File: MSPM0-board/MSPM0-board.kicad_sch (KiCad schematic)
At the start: 13 parts, among them J1 USB_C_Receptacle_USB2.0_16P, U1 MSPM0G3507SPTR, U2 USBLC6-2SC6, X1 8MHz

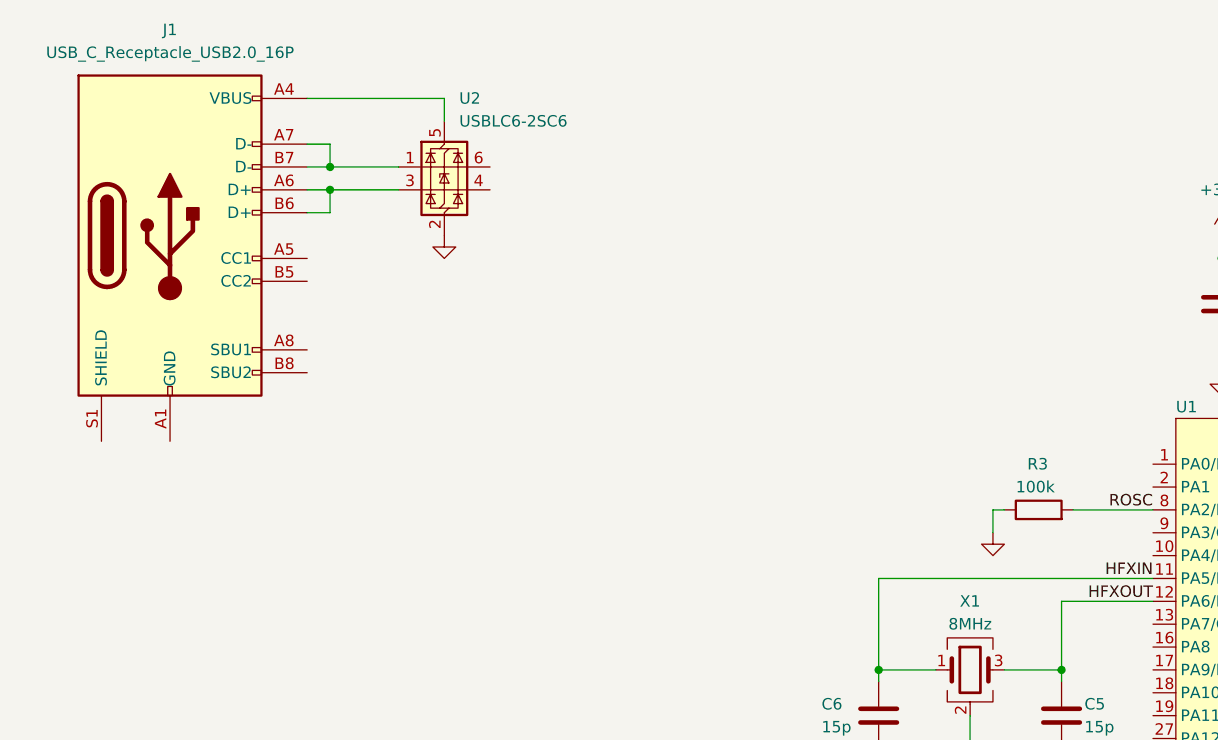
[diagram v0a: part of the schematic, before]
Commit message: mspm0(feat): add power supply circuit
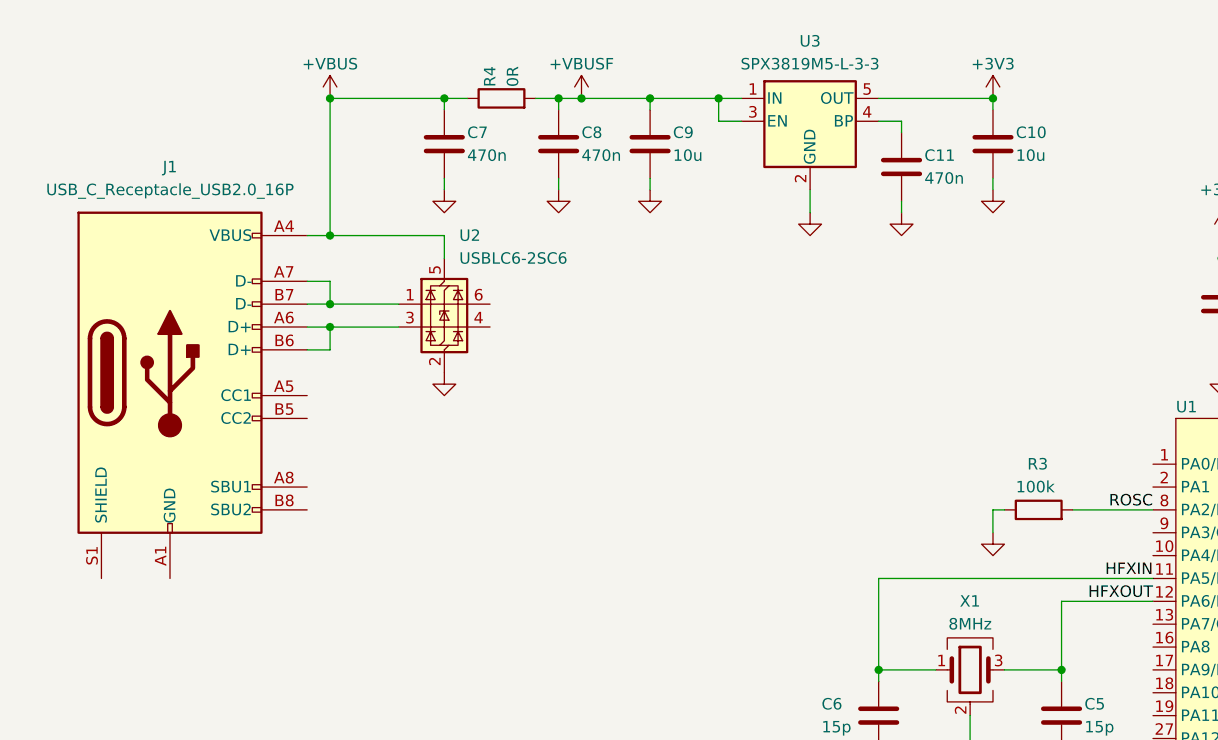
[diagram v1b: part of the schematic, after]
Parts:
- added C10, C9: 10u, Capacitor_SMD:C_0805_2012Metric, symbol Device:C
- added C11, C7, C8: 470n, Capacitor_SMD:C_0603_1608Metric, symbol Device:C
- added R4: 0R, Resistor_SMD:R_0603_1608Metric, symbol Device:R
- added U3: SPX3819M5-L-3-3, Package_TO_SOT_SMD:SOT-23-5, symbol Regulator_Linear:SPX3819M5-L-3-3
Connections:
- net +3V3: now also C10.1, U3.5 (OUT)
- net GND: now also C10.2, C11.2, C7.2, C8.2, C9.2, U3.2 (GND)
- net +VBUS: now reaches J1.A4 (VBUS), J1.A9 (VBUS), J1.B4 (VBUS), J1.B9 (VBUS), U2.5 (VBUS)
- net +VBUS: now also C7.1, R4.1
- new net: C11.1, U3.4 (BP)
- new net +VBUSF: C8.1, C9.1, R4.2, U3.1 (IN), U3.3 (EN)
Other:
- moved on the sheet: J1, U2

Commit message: mspm0(feat): finish usb
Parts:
- added R5, R6: 5k1, Resistor_SMD:R_0603_1608Metric, symbol Device:R
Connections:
- net GND: now also J1.A1 (GND), J1.A12 (GND), J1.B1 (GND), J1.B12 (GND), J1.S1 (SHIELD), R5.2, R6.2
- net at J1.A5 (CC1): now also R6.1
- net USBD+: now reaches J1.A6 (D+), J1.B6 (D+), U2.3 (I/O2)
- net USBD-: now reaches J1.A7 (D-), J1.B7 (D-), U2.1 (I/O1)
- net at J1.B5 (CC2): now also R5.1
- no-connect marks 0 -> 2
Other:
- moved on the sheet: U2

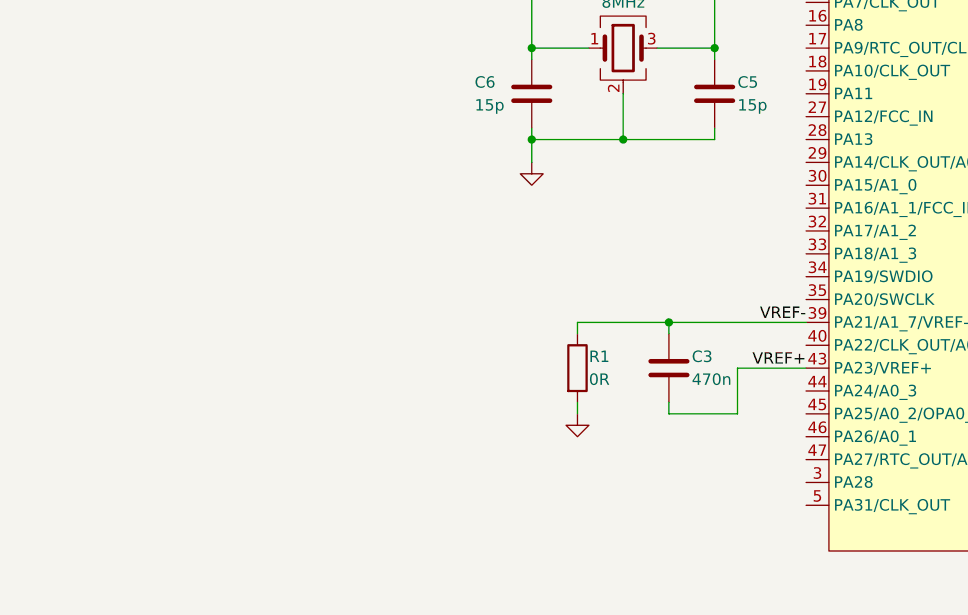
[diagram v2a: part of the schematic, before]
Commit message: mspm0(feat): add swd connector
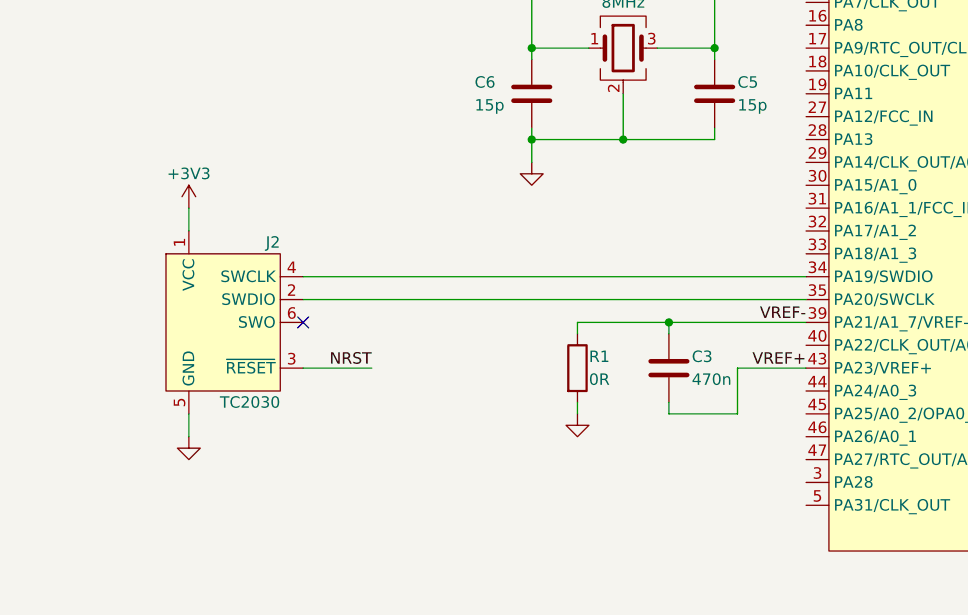
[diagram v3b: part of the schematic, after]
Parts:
- added J2: TC2030, Connector:Tag-Connect_TC2030-IDC-FP_2x03_P1.27mm_Vertical, symbol Connector:Conn_ARM_SWD_TagConnect_TC2030
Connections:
- net +3V3: now also J2.1 (VCC)
- net GND: now also J2.5 (GND)
- net NRST: now also J2.3 (~{RESET})
- net at U1.34 (PA19/SWDIO): now also J2.4 (SWCLK)
- net at U1.35 (PA20/SWCLK): now also J2.2 (SWDIO)
- no-connect marks 2 -> 3

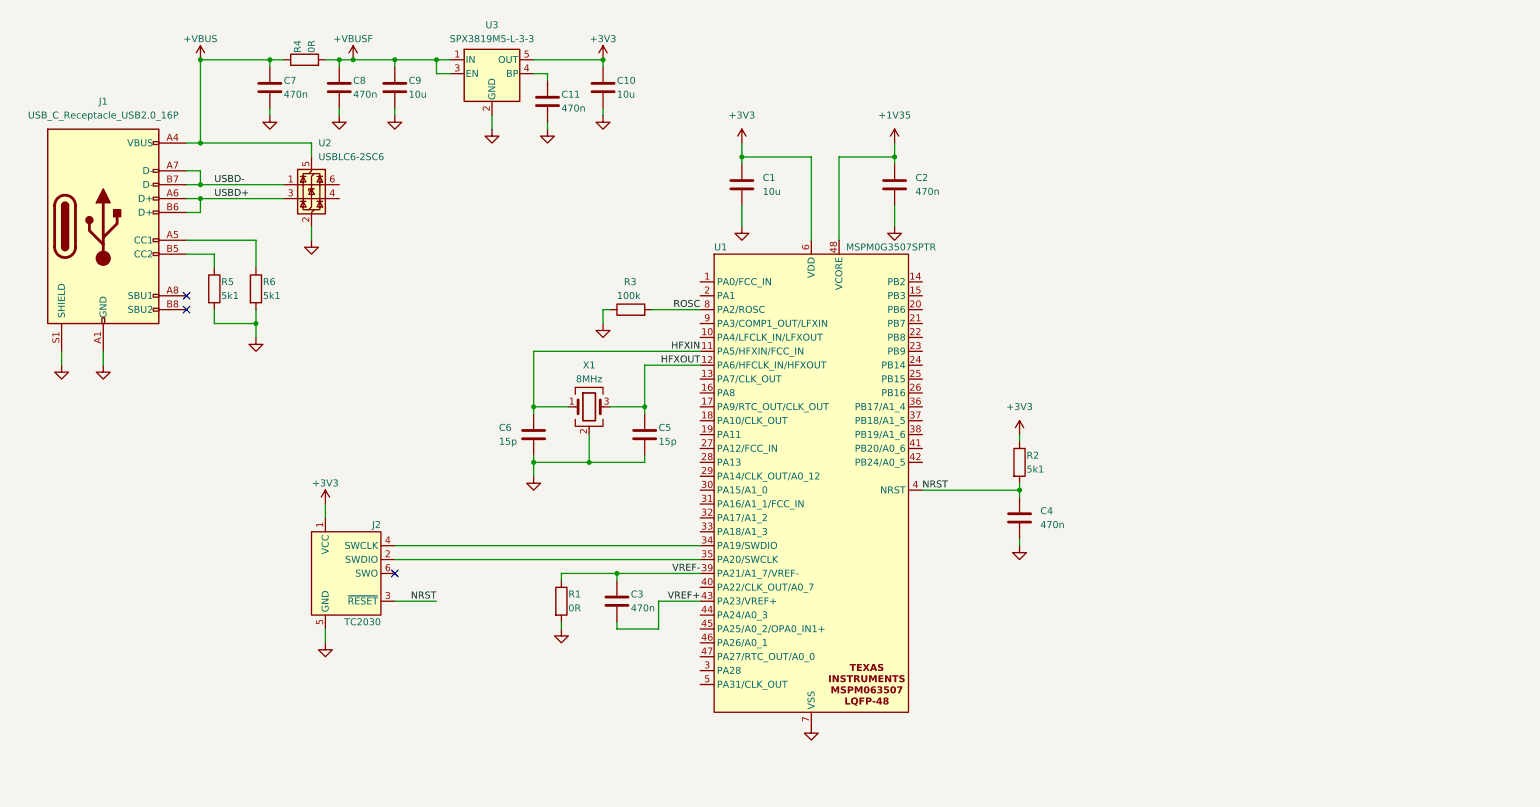
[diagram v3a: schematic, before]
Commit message: mspm0(feat): add usb to uart converter
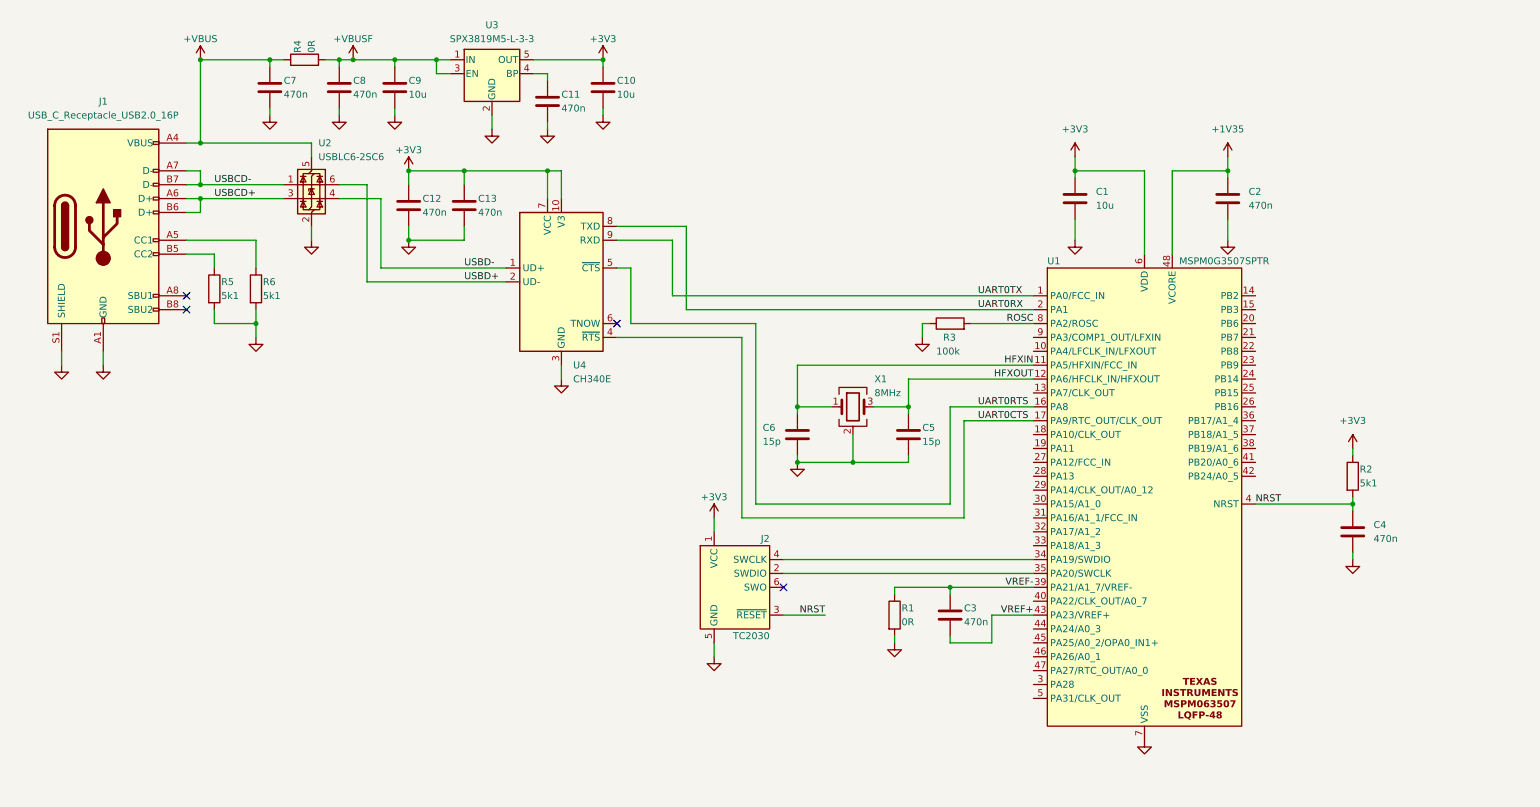
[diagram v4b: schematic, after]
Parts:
- added C12, C13: 470n, Capacitor_SMD:C_0603_1608Metric, symbol Device:C
- added U4: CH340E, Package_SO:MSOP-10_3x3mm_P0.5mm, symbol Interface_USB:CH340E
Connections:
- net +3V3: now also C12.1, C13.1, U4.10 (V3), U4.7 (VCC)
- net GND: now also C12.2, C13.2, U4.3 (GND)
- net USBD+: now also U2.6 (I/O1), U4.2 (UD-); no longer J1.A6 (D+), J1.B6 (D+), U2.3 (I/O2)
- net USBD-: now also U2.4 (I/O2), U4.1 (UD+); no longer J1.A7 (D-), J1.B7 (D-), U2.1 (I/O1)
- net UART0TX: now reaches U1.1 (PA0/FCC_IN)
- net UART0TX: now also U4.9 (RXD)
- net UART0RTS: now reaches U1.16 (PA8)
- net UART0RTS: now also U4.5 (~{CTS})
- net UART0CTS: now reaches U1.17 (PA9/RTC_OUT/CLK_OUT)
- net UART0CTS: now also U4.4 (~{RTS})
- net UART0RX: now reaches U1.2 (PA1)
- net UART0RX: now also U4.8 (TXD)
- new net USBCD+: J1.A6 (D+), J1.B6 (D+), U2.3 (I/O2)
- new net USBCD-: J1.A7 (D-), J1.B7 (D-), U2.1 (I/O1)
- no-connect marks 3 -> 4
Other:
- moved on the sheet: C1, C2, C3, C4, C5, C6, J2, R1, R2, R3, U1, X1

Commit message: mspm0(feat): add accelerometer
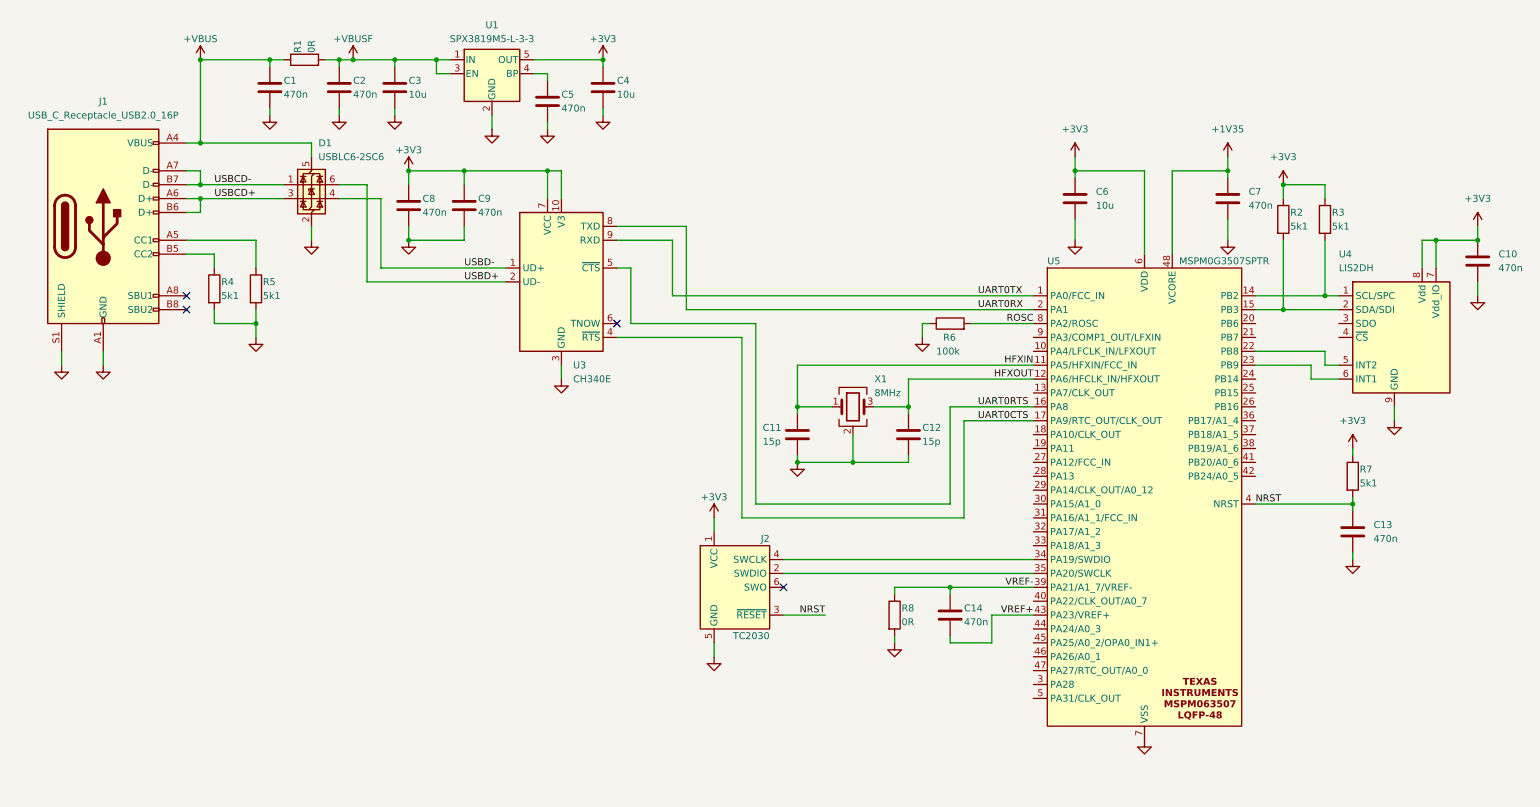
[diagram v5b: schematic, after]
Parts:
- added C10: 470n, Capacitor_SMD:C_0603_1608Metric, symbol Device:C
- added R2, R3: 5k1, Resistor_SMD:R_0603_1608Metric, symbol Device:R
- added U4: LIS2DH, Package_LGA:LGA-14_2x2mm_P0.35mm_LayoutBorder3x4y, symbol Sensor_Motion:LIS2DH
- renumbered C7 to C1, C6 to C11, C5 to C12, C4 to C13, C3 to C14, C8 to C2, C9 to C3, C10 to C4, C11 to C5, C1 to C6, C2 to C7, C12 to C8, C13 to C9, U2 to D1, R4 to R1, R5 to R4, R6 to R5, R3 to R6, R2 to R7, R1 to R8, U3 to U1, U4 to U3, U1 to U5
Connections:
- net +3V3: now also C10.1, R2.1, R3.1, U4.7 (Vdd_IO), U4.8 (Vdd)
- net GND: now also C10.2, U4.10 (GND), U4.11 (GND), U4.12 (GND), U4.13 (GND), U4.14 (GND), U4.9 (GND)
- net at U5.14 (PB2): now also R3.2, U4.1 (SCL/SPC)
- net at U5.15 (PB3): now also R2.2, U4.2 (SDA/SDI)
- net at U5.22 (PB8): now also U4.5 (INT2)
- net at U5.23 (PB9): now also U4.6 (INT1)

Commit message: mspm0(feat): clean the schematic and generate outputs
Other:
- note added: "+3V3 LDO Regulator"
- note added: "Accelerometer"
- note added: "MSPM0 Microcontroller"
- note added: "SWD Header"
- note added: "USB-C CONNECTOR"
- note added: "USB-UART Converter"
- moved on the sheet: C1, C10, C11, C12, C13, C14, C2, C3, C4, C5, C6, C7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
